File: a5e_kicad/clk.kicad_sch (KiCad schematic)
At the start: 18 parts, among them U9 AX3DAF1-100.0000T, Y2 SIT8924BA-73-18N-25.000000, Y4 OT3225100MJBA4SL 100MHz

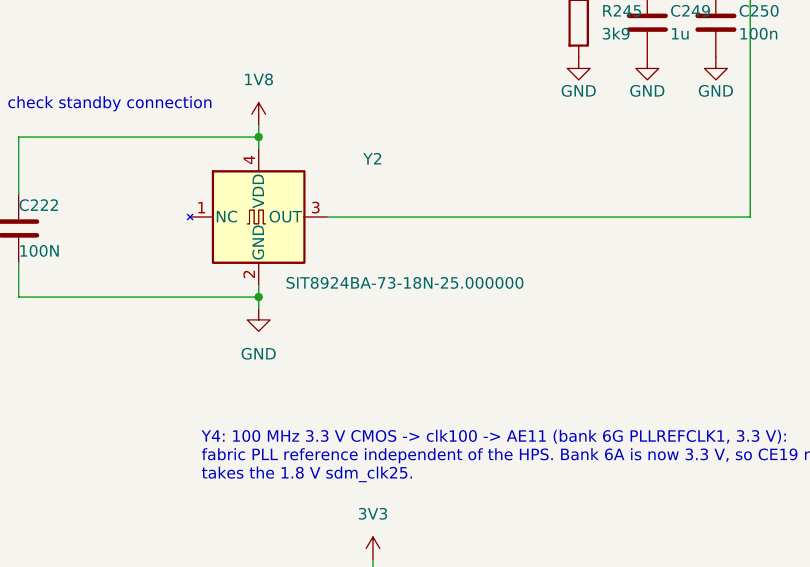
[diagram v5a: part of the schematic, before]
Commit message: Add jlc-tools submodule; fix two parts JLC can't supply
- tools/jlc: johonkanen/jlc-tools (06e4105). Part search, BOM stock
  check, BOM/CPL and fab outputs, as on the Agilex 3 card.
- The stock check (orderable quantity, 10 boards) found:
  - R56 560k (C132339) oversold, min buy 10000. R56 is now DNP and R57
    is a single 60.4k 1% (C25911): the TDA38812 data sheet value for
    1 MHz FCCM, same as the old 560k||68k = 60.6k.
  - Y2 SIT8924BA-73-18N (C17359088): 0 free. Changed to
    SIT8924BA-78-18E (C17247134, 1000 free), same 2016 footprint. Pin 1
    is OE on this variant and is left open (output enabled).
- Still open: J9 RJ45 RB1-125B8G1A (C363353) is oversold.
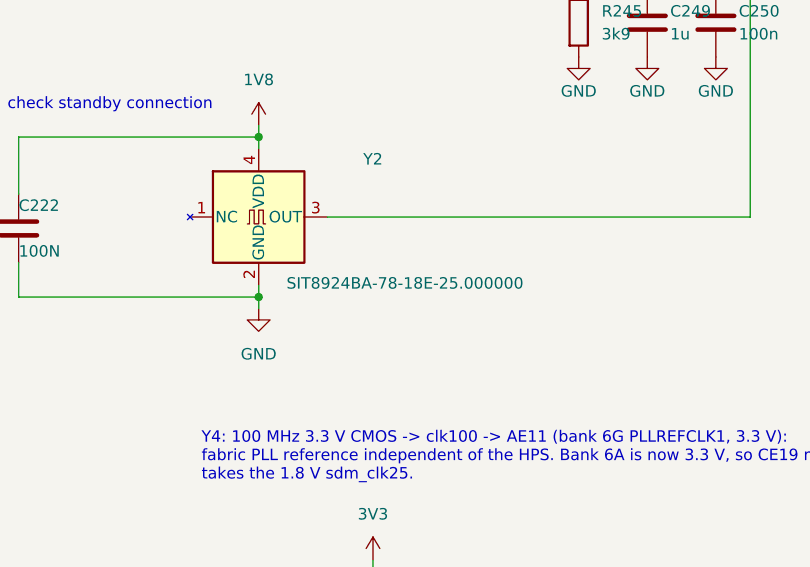
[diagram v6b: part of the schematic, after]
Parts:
- Y2: value SIT8924BA-73-18N-25.000000 -> SIT8924BA-78-18E-25.000000; LCSC C17359088 -> C17247134
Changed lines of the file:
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@@
 			)
 		)
-		(property "Value" "SIT8924BA-73-18N-25.000000"
+		(property "Value" "SIT8924BA-78-18E-25.000000"
 			(at 124.206 116.586 0)
 			(show_name no)
@@
 			)
 		)
-		(property "LCSC" "C17359088"
+		(property "LCSC" "C17247134"
 			(at 125.73 118.11 0)
 			(hide yes)

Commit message: clk: LPDDR4 refclk network (R25-R28, R244, R245, C8, C9, C249, C250) to 0201
Footprints to R_0201_0603Metric / C_0201_0603Metric (R25 had a C_0402 footprint),
LCSC: 33R C320843, 49.9R C170197, 1k C270365, 3k9 C473550, 1u C272877 (6.3 V),
100n C190183. Netlist connections unchanged. PCB still needs Update from Schematic.
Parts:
- C249: footprint Capacitor_SMD:C_0402_1005Metric -> Capacitor_SMD:C_0201_0603Metric; LCSC C52923 -> C272877
- C250, C8, C9: footprint Capacitor_SMD:C_0402_1005Metric -> Capacitor_SMD:C_0201_0603Metric; LCSC C1525 -> C190183
- R244: footprint Resistor_SMD:R_0402_1005Metric -> Resistor_SMD:R_0201_0603Metric; LCSC C11702 -> C270365
- R245: footprint Resistor_SMD:R_0402_1005Metric -> Resistor_SMD:R_0201_0603Metric; LCSC C51721 -> C473550
- R25: footprint Capacitor_SMD:C_0402_1005Metric -> Resistor_SMD:R_0201_0603Metric; LCSC C25105 -> C320843
- R26: footprint Resistor_SMD:R_0402_1005Metric -> Resistor_SMD:R_0201_0603Metric; LCSC C25105 -> C320843
- R27, R28: footprint Resistor_SMD:R_0402_1005Metric -> Resistor_SMD:R_0201_0603Metric; LCSC C25120 -> C170197
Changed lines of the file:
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@@
 			)
 		)
-		(property "Footprint" "Capacitor_SMD:C_0402_1005Metric"
+		(property "Footprint" "Capacitor_SMD:C_0201_0603Metric"
 			(at 143.51 58.7248 0)
 			(hide yes)
@@
 			)
 		)
-		(property "LCSC" "C1525"
+		(property "LCSC" "C190183"
 			(at 143.51 58.7248 0)
 			(hide yes)
@@
 			)
 		)
-		(property "Footprint" "Resistor_SMD:R_0402_1005Metric"
+		(property "Footprint" "Resistor_SMD:R_0201_0603Metric"
 			(at 120.65 61.468 90)
 			(hide yes)
@@
 			)
 		)
-		(property "LCSC" "C25105"
+		(property "LCSC" "C320843"
 			(at 120.65 61.468 90)
 			(hide yes)
@@
 			)
 		)
-		(property "Footprint" "Capacitor_SMD:C_0402_1005Metric"
+		(property "Footprint" "Capacitor_SMD:C_0201_0603Metric"
 			(at 143.51 53.6448 0)
 			(hide yes)
@@
 			)
 		)
-		(property "LCSC" "C1525"
+		(property "LCSC" "C190183"
 			(at 143.51 53.6448 0)
 			(hide yes)
@@
 			)
 		)
-		(property "Footprint" "Capacitor_SMD:C_0402_1005Metric"
+		(property "Footprint" "Capacitor_SMD:C_0201_0603Metric"
 			(at 151.13 87.63 0)
 			(hide yes)
@@
 			)
 		)
-		(property "LCSC" "C52923"
+		(property "LCSC" "C272877"
 			(at 151.13 87.63 0)
 			(hide yes)
@@
 			)
 		)
-		(property "Footprint" "Resistor_SMD:R_0402_1005Metric"
+		(property "Footprint" "Resistor_SMD:R_0201_0603Metric"
 			(at 135.89 80.01 0)
 			(hide yes)
@@
 			)
 		)
-		(property "LCSC" "C11702"
+		(property "LCSC" "C270365"
 			(at 135.89 80.01 0)
 			(hide yes)
@@
 			)
 		)
-		(property "Footprint" "Resistor_SMD:R_0402_1005Metric"
+		(property "Footprint" "Resistor_SMD:R_0201_0603Metric"
 			(at 149.098 67.31 90)
 			(hide yes)
@@
 			)
 		)
-		(property "LCSC" "C25120"
+		(property "LCSC" "C170197"
 			(at 149.098 67.31 90)
 			(hide yes)
@@
 			)
 		)
-		(property "Footprint" "Resistor_SMD:R_0402_1005Metric"
+		(property "Footprint" "Resistor_SMD:R_0201_0603Metric"
 			(at 157.988 67.31 90)
 			(hide yes)
@@
 			)
 		)
-		(property "LCSC" "C25120"
+		(property "LCSC" "C170197"
 			(at 157.988 67.31 90)
 			(hide yes)
@@
 			)
 		)
-		(property "Footprint" "Resistor_SMD:R_0402_1005Metric"
+		(property "Footprint" "Resistor_SMD:R_0201_0603Metric"
 			(at 143.51 87.63 0)
 			(hide yes)
@@
 			)
 		)
-		(property "LCSC" "C51721"
+		(property "LCSC" "C473550"
 			(at 143.51 87.63 0)
 			(hide yes)
@@
 			)
 		)
-		(property "Footprint" "Capacitor_SMD:C_0402_1005Metric"
+		(property "Footprint" "Resistor_SMD:R_0201_0603Metric"
 			(at 120.65 56.388 90)
 			(hide yes)
@@
 			)
 		)
-		(property "LCSC" "C25105"
+		(property "LCSC" "C320843"
 			(at 120.65 56.388 90)
 			(hide yes)
@@
 			)
 		)
-		(property "Footprint" "Capacitor_SMD:C_0402_1005Metric"
+		(property "Footprint" "Capacitor_SMD:C_0201_0603Metric"
 			(at 158.75 87.63 0)
 			(hide yes)
@@
 			)
 		)
-		(property "LCSC" "C1525"
+		(property "LCSC" "C190183"
 			(at 158.75 87.63 0)
 			(hide yes)
